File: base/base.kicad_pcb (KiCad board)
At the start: 2 copper layers, 105 x 100 mm, 26 parts, among them J1 USB_OTG, SW1 SW_Push, U1 Z80CPU, U2 27C256, U3 7404, U4 55257, U5 7432, U6 16550, U7 FT230XS, X1 4 MHz

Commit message: Layout work
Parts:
- added J2: CONN_02X20, Pin_Headers:Pin_Header_Straight_2x20_Pitch2.54mm, F.Cu at (174.4, 65.6)
- added X2: 4 MHz, Oscillators:Oscillator_DIP-8, F.Cu at (219.9, 74.5)
- moved X1 156.3 mm to (206.4, 74.5)
- moved D1 146.8 mm to (199.7, 91.7), turned to 0 degrees
- moved C3 146.4 mm to (193.1, 88.6), turned to 0 degrees
- moved SW1 142.1 mm to (185.1, 88.9)
- moved R1 139.1 mm to (191.3, 95.8), turned to 0 degrees
- moved U3 121.0 mm to (182.6, 65.6), turned to 0 degrees
- moved C1 120.7 mm to (182.7, 96.1)
- moved U5 114.2 mm to (193.9, 65.6), turned to 0 degrees
- moved C2 83.8 mm to (186.6, 96.1)
- moved U7 66.0 mm to (208.7, 85.5)
- moved C4 59.9 mm to (182.7, 101.3)
- moved C5 56.8 mm to (199.8, 86.7)
- moved U6 50.6 mm to (144.8, 144.8), turned to 180 degrees
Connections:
- U1 pad 20: Net-(U1-Pad20) -> IORQ
- U3 pad 8: (no net) -> Net-(U3-Pad8)
- U3 pad 9: (no net) -> /A7
- U5 pad 10: (no net) -> Net-(U3-Pad8)
- U5 pad 3: ROM_CE -> RAM_CE
- U5 pad 6: RAM_CE -> ROM_CE
- U5 pad 8: (no net) -> UART_CE
- U5 pad 9: (no net) -> IORQ
- U6 pad 12: Net-(U6-Pad12) -> +5V
- U6 pad 13: Net-(U6-Pad13) -> +5V
- U6 pad 14: Net-(U6-Pad14) -> UART_CE
- U6 pad 18: Net-(U6-Pad18) -> WR
- U6 pad 19: Net-(U6-Pad19) -> GND
- U6 pad 21: Net-(U6-Pad21) -> RD
- U6 pad 22: Net-(U6-Pad22) -> GND
- U6 pad 25: Net-(U6-Pad25) -> GND
- U6 pad 26: Net-(U6-Pad26) -> /A2
- U6 pad 27: Net-(U6-Pad27) -> /A1
- U6 pad 28: Net-(U6-Pad28) -> /A0
- U6 pad 9: Net-(U6-Pad9) -> Net-(U6-Pad15)
- U7 pad 1: Net-(U7-Pad1) -> Net-(U6-Pad11)
- U7 pad 4: Net-(U7-Pad4) -> Net-(U6-Pad10)
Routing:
- net WR: track 0.00 -> 111.5 mm, vias 0 -> 1
- net /D2: track 0.00 -> 108.2 mm, vias 0 -> 1
- net /D0: track 0.00 -> 106.6 mm, vias 0 -> 1
- net /D1: track 0.00 -> 101.8 mm, vias 0 -> 1
- net RD: track 0.00 -> 100.5 mm, vias 0 -> 1
- net /D4: track 0.00 -> 96.4 mm, vias 0 -> 1
- net /D3: track 0.00 -> 96.4 mm, vias 0 -> 1
- net /D5: track 0.00 -> 93.1 mm, vias 0 -> 1
- net /D6: track 0.00 -> 88.4 mm, vias 0 -> 1
- net /D7: track 0.00 -> 87.3 mm, vias 0 -> 1
- net /A11: track 0.00 -> 71.7 mm, vias 0 -> 1
- net /A13: track 0.00 -> 61.6 mm
- net /A10: track 0.00 -> 57.5 mm, vias 0 -> 1
- net /A9: track 0.00 -> 53.2 mm, vias 0 -> 1
- net /A14: track 0.00 -> 51.6 mm, vias 0 -> 1
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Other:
- net class Default: clearance 0.2 -> 0.152; trace_width 0.25 -> 0.152; via_dia 0.8 -> 0.6; via_drill 0.4 -> 0.3
- rule trace_clearance: 0.2 -> 0.152
- rule trace_min: 0.2 -> 0.152
- rule via_min_size: 0.4 -> 0.3

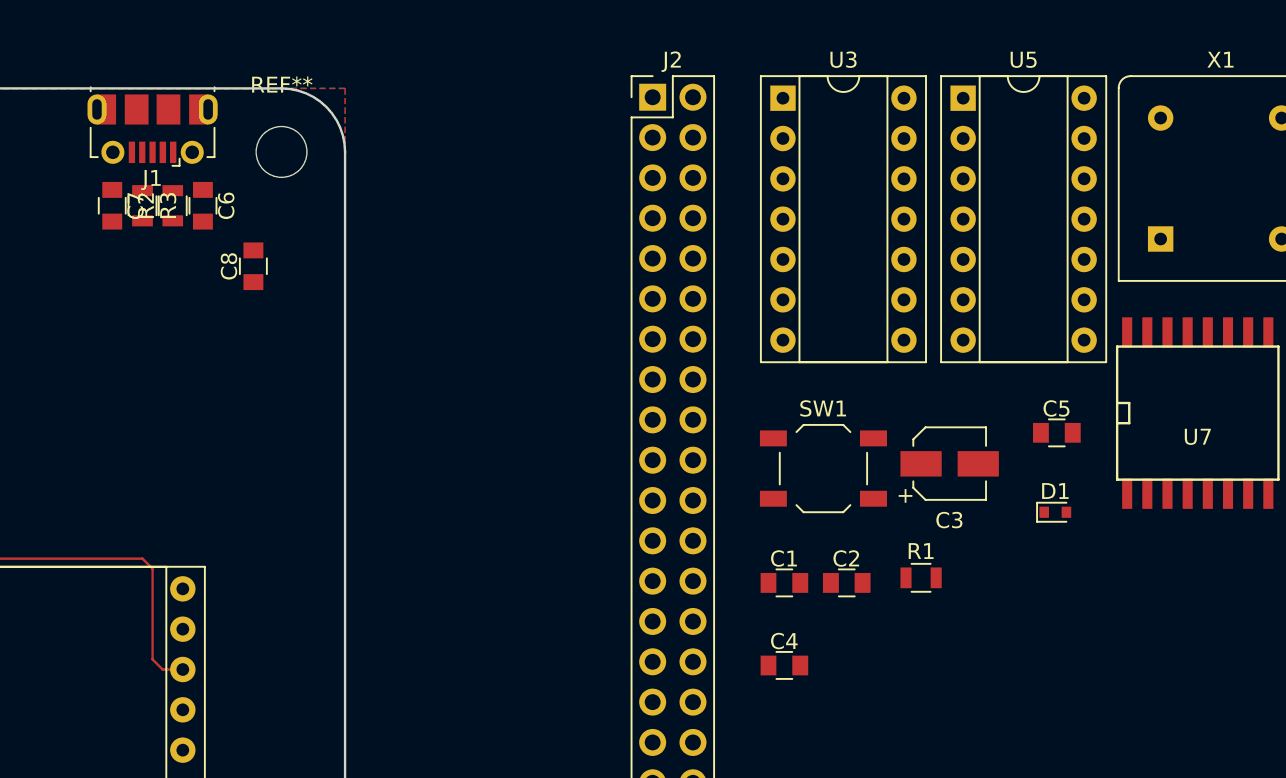
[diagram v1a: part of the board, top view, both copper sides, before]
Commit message: Replaced SMD passives with THT
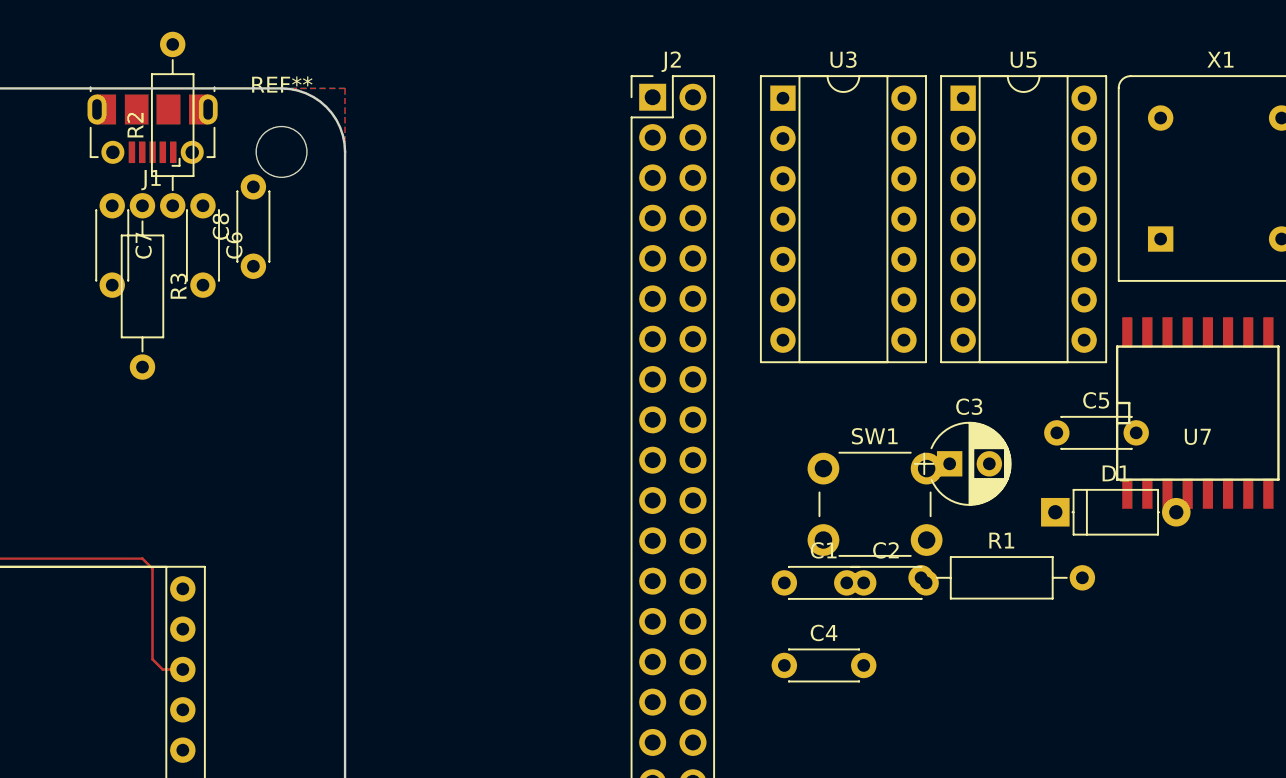
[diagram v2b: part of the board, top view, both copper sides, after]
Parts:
- C1, C2, C4, C5, C6, C7, C8: footprint Capacitors_SMD:C_0805 -> Capacitors_THT:C_Disc_D4.3mm_W1.9mm_P5.00mm
- C3: footprint Capacitors_SMD:CP_Elec_4x4.5 -> Capacitors_THT:CP_Radial_D5.0mm_P2.50mm
- D1: footprint Diodes_SMD:D_SOD-523 -> Diodes_THT:D_A-405_P7.62mm_Horizontal
- R1, R2, R3: footprint Resistors_SMD:R_0805 -> Resistors_THT:R_Axial_DIN0207_L6.3mm_D2.5mm_P10.16mm_Horizontal
- SW1: footprint Buttons_Switches_SMD:SW_SPST_TL3342 -> Buttons_Switches_THT:SW_PUSH_6mm_h5mm
- X2: value 4 MHz -> 1.8432 MHz

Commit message: Further layout work
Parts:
- removed C2, C4: 1 uF, Capacitors_THT:C_Disc_D4.3mm_W1.9mm_P5.00mm
- removed C6, C7: 47 nF, Capacitors_THT:C_Disc_D4.3mm_W1.9mm_P5.00mm
- removed C8: 100 nF, Capacitors_THT:C_Disc_D4.3mm_W1.9mm_P5.00mm
- removed J2: CONN_02X20, Pin_Headers:Pin_Header_Straight_2x20_Pitch2.54mm
- removed R2, R3: 27, Resistors_THT:R_Axial_DIN0207_L6.3mm_D2.5mm_P10.16mm_Horizontal
- removed U7: FT230XS, SMD_Packages:SO-16-L
- added JP1: CLK JMP, Pin_Headers:Pin_Header_Angled_1x02_Pitch2.54mm, F.Cu at (62.2, 154.3)
- J1: value USB_OTG -> FTDI; footprint Connectors_USB:USB_Micro-B_Molex-105017-0001 -> Pin_Headers:Pin_Header_Angled_1x06_Pitch2.54mm
- moved X1 151.5 mm to (74.9, 149.9), turned to 180 degrees
- moved D1 126.0 mm to (88.3, 150.5), turned to 180 degrees
- moved SW1 125.8 mm to (80.0, 158.1)
- moved C1 124.9 mm to (61.6, 127.0), turned to 90 degrees
- moved C3 124.9 mm to (91.4, 161.3), turned to 90 degrees
- moved R1 117.4 mm to (89.5, 154.3), turned to 180 degrees
- moved X2 109.2 mm to (141.0, 149.9), turned to 180 degrees
- moved U3 108.1 mm to (101.6, 137.2), turned to 270 degrees
- moved U5 101.5 mm to (121.9, 137.2), turned to 270 degrees
- moved C5 99.0 mm to (122.6, 148.6)
- moved J1 88.8 mm to (128.3, 154.3), turned to 270 degrees
- moved U2 2.54 mm to (86.4, 96.5)
- moved U1 2.54 mm to (66.0, 96.5)
- moved U4 2.54 mm to (106.7, 96.5)
- moved U6 2.54 mm to (142.2, 144.8)
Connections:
- net A15 renamed /A15
- J1 pad 1: +5V -> GND
- J1 pad 2: Net-(C6-Pad1) -> CTS
- J1 pad 3: Net-(C7-Pad1) -> +5V
- J1 pad 4: Net-(J1-Pad4) -> TX
- J1 pad 5: GND -> RX
- J1 pad 6: GND -> RTS
- U1 pad 6: Net-(U1-Pad6) -> Net-(JP1-Pad2)
- U2 pad 28: VCC -> +5V
- U4 pad 28: VCC -> +5V
- U6 pad 10: Net-(U6-Pad10) -> TX
- U6 pad 11: Net-(U6-Pad11) -> RX
- U6 pad 35: Net-(U6-Pad35) -> RESET
- X1 pad 5: Net-(U1-Pad6) -> Net-(JP1-Pad1)
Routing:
- net +5V: track 0.00 -> 304.9 mm
- net UART_CE: track 0.00 -> 82.5 mm
- net /A7: track 27.5 -> 108.3 mm, vias 0 -> 1
- net /A15: track 0.00 -> 80.8 mm
- net MREQ: track 0.00 -> 75.7 mm
- net RX: track 0.00 -> 65.7 mm
- net Net-(U6-Pad16): track 0.00 -> 64.2 mm
- net Net-(C3-Pad1): track 0.00 -> 60.7 mm
- net TX: track 0.00 -> 56.7 mm
- net Net-(JP1-Pad2): track 0.00 -> 51.2 mm, vias 0 -> 1
- net IORQ: track 0.00 -> 47.1 mm
- net RAM_CE: track 0.00 -> 40.2 mm
- net Net-(U3-Pad6): track 0.00 -> 34.4 mm
- net RESET: track 0.00 -> 33.7 mm
- net Net-(U3-Pad8): track 0.00 -> 29.9 mm
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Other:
- net class VCC added: clearance 0.3, trace_width 0.3, via_dia 0.6, via_drill 0.3

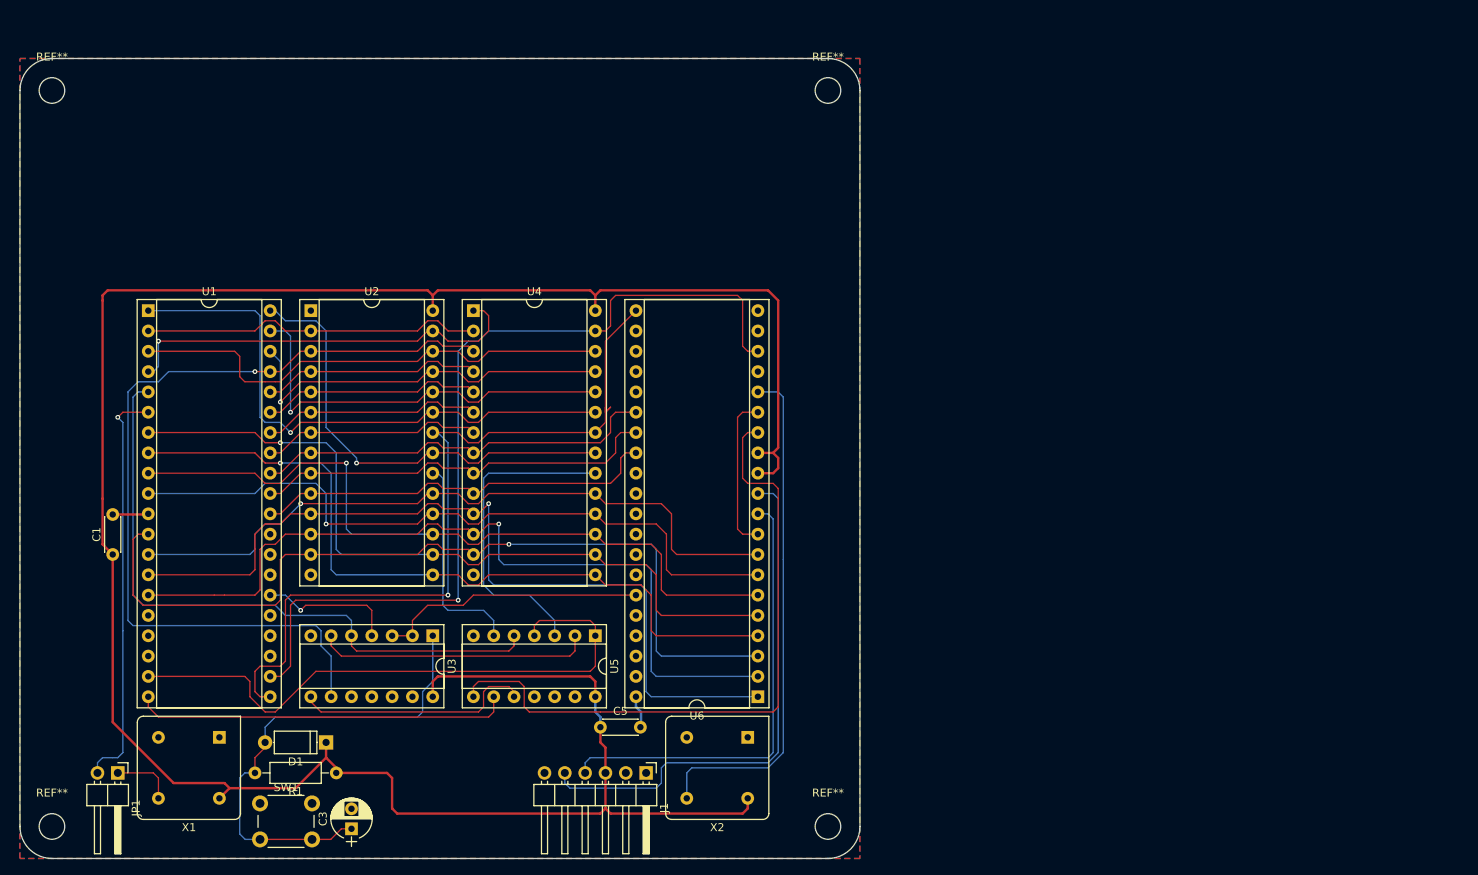
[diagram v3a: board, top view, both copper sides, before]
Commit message: Started layout of RC2014 header
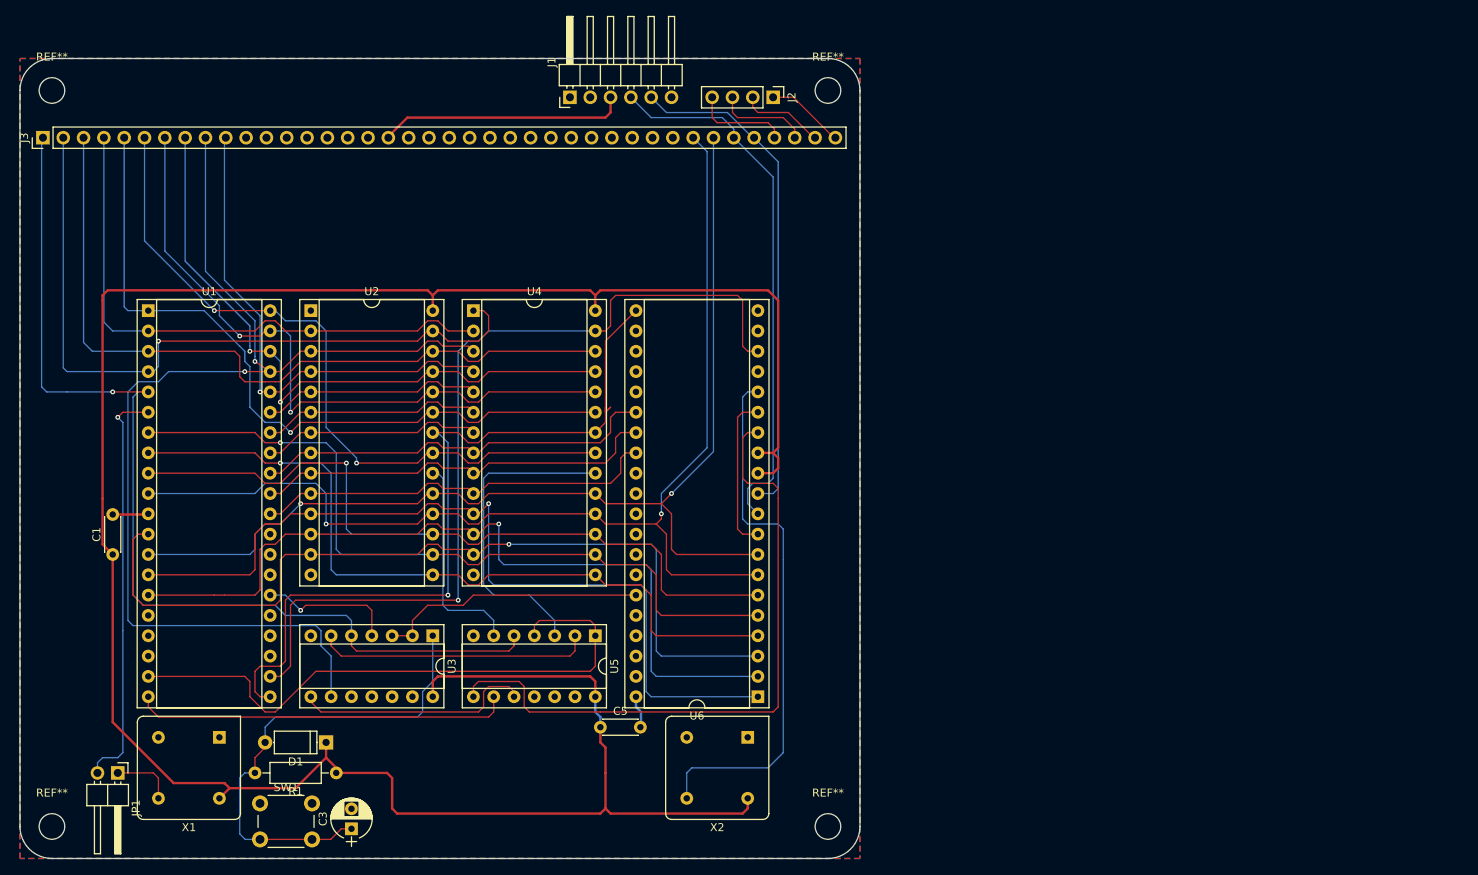
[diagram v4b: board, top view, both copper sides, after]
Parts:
- added J2: CONN_01X04, Pin_Headers:Pin_Header_Straight_1x04_Pitch2.54mm, F.Cu at (144.1, 69.8)
- added J3: CONN_01X40, Pin_Headers:Pin_Header_Straight_1x40_Pitch2.54mm, F.Cu at (52.9, 74.9)
- moved J1 85.0 mm to (118.7, 69.8), turned to 90 degrees
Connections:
- net Net-(JP1-Pad2) renamed CLOCK
- U1 pad 16: Net-(U1-Pad16) -> INT
- U1 pad 27: Net-(U1-Pad27) -> M1
- U6 pad 30: Net-(U6-Pad30) -> INT
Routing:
- net /D6: track 88.4 -> 140.0 mm, vias 1 -> 2
- net /D7: track 87.3 -> 135.7 mm, vias 1 -> 2
- net /A15: track 80.8 -> 125.7 mm, vias 0 -> 1
- net /A14: track 51.6 -> 91.2 mm
- net /A6: track 27.5 -> 62.5 mm, vias 0 -> 1
- net /A13: track 61.6 -> 95.7 mm
- net /A8: track 48.9 -> 81.7 mm, vias 1 -> 2
- net /A7: track 108.3 -> 141.2 mm, vias 1 -> 2
- net /A9: track 53.2 -> 85.9 mm, vias 1 -> 2
- net /A10: track 57.5 -> 90.0 mm, vias 1 -> 2
- net +5V: track 304.9 -> 336.2 mm
- net /A12: track 42.7 -> 71.8 mm
- net /A11: track 71.7 -> 92.4 mm
- net Net-(J2-Pad4): track 0.00 -> 12.0 mm
- net Net-(J2-Pad3): track 0.00 -> 11.6 mm
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
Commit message: Finished board layout
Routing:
- net INT: track 0.00 -> 150.5 mm, vias 0 -> 3
- net IORQ: track 47.1 -> 166.1 mm, vias 0 -> 2
- net MREQ: track 75.7 -> 185.3 mm, vias 0 -> 2
- net M1: track 0.00 -> 77.6 mm, vias 0 -> 1
- net RESET: track 33.7 -> 105.5 mm, vias 0 -> 3
- net CLOCK: track 51.2 -> 122.7 mm, vias 1 -> 3
- net /D3: track 96.4 -> 163.6 mm, vias 1 -> 2
- net /D4: track 96.4 -> 162.9 mm, vias 1 -> 2
- net /D5: track 93.1 -> 159.4 mm, vias 1 -> 2
- net /D2: track 108.2 -> 170.0 mm, vias 1 -> 2
- net /D1: track 101.8 -> 159.2 mm, vias 1 -> 2
- net /D0: track 106.6 -> 161.0 mm
- net +5V: track 336.2 -> 390.4 mm
- net /A0: track 51.0 -> 103.0 mm, vias 0 -> 1
- net /A1: track 51.0 -> 102.6 mm, vias 0 -> 1
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
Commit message: Changed FTDI and CLK_JMP footprint
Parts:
- J1: footprint Pin_Headers:Pin_Header_Angled_1x06_Pitch2.54mm -> Pin_Headers:Pin_Header_Straight_1x06_Pitch2.54mm
- JP1: footprint Pin_Headers:Pin_Header_Angled_1x02_Pitch2.54mm -> Pin_Headers:Pin_Header_Straight_1x02_Pitch2.54mm
- moved JP1 3.24 mm to (62.9, 157.5), turned to 180 degrees
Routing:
- net Net-(JP1-Pad1): track 7.88 -> 4.45 mm
- net CLOCK: track 122.7 -> 120.9 mm
